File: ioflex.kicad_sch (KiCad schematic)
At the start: 2 parts, among them CN10 DF40C-40DP-0.4V, CN11 DF40C-40DP-0.4V

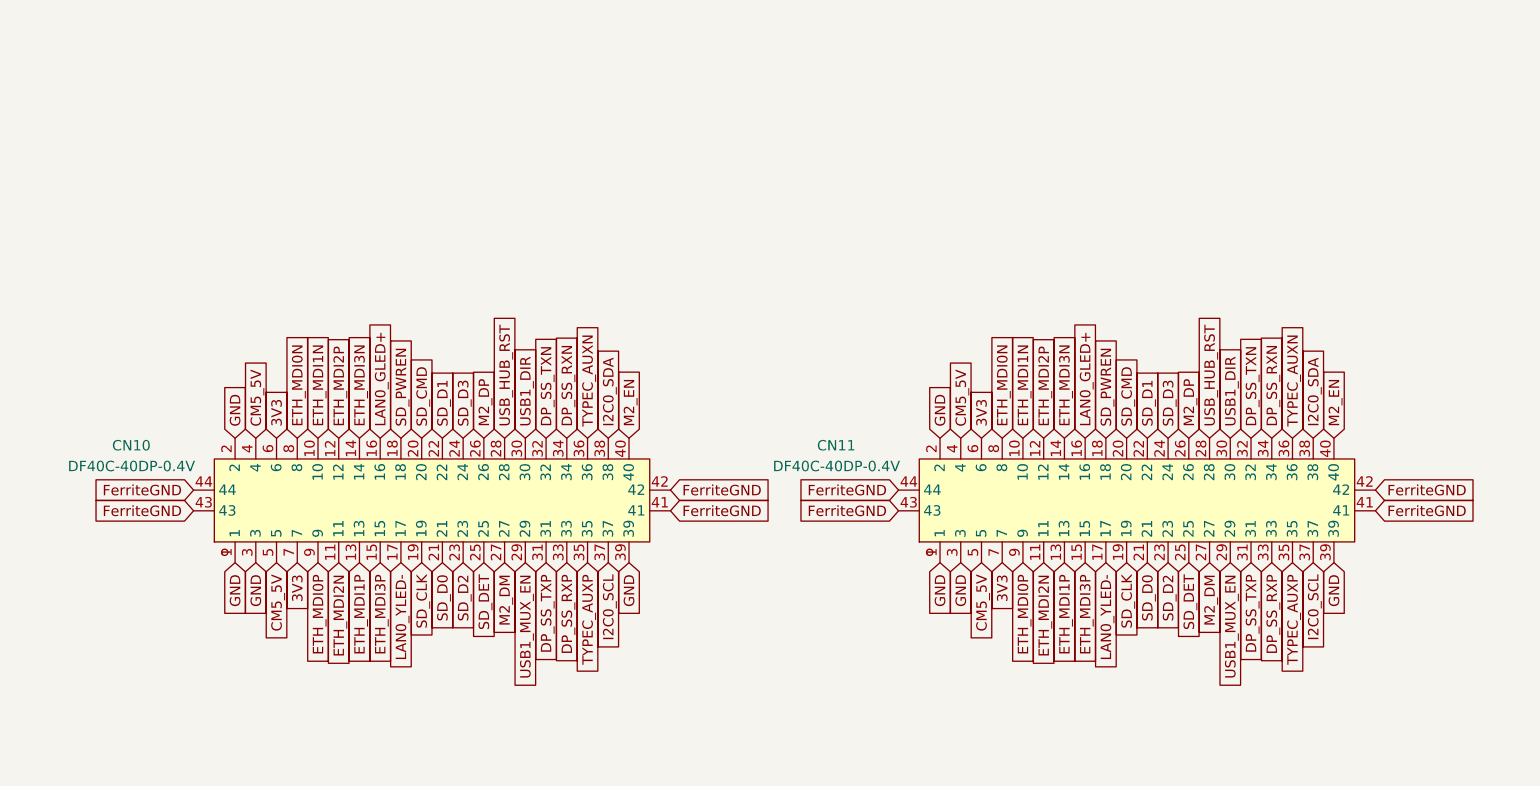
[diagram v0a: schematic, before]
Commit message: finish wiring up usb hub + fix stale nets + address DRC errors
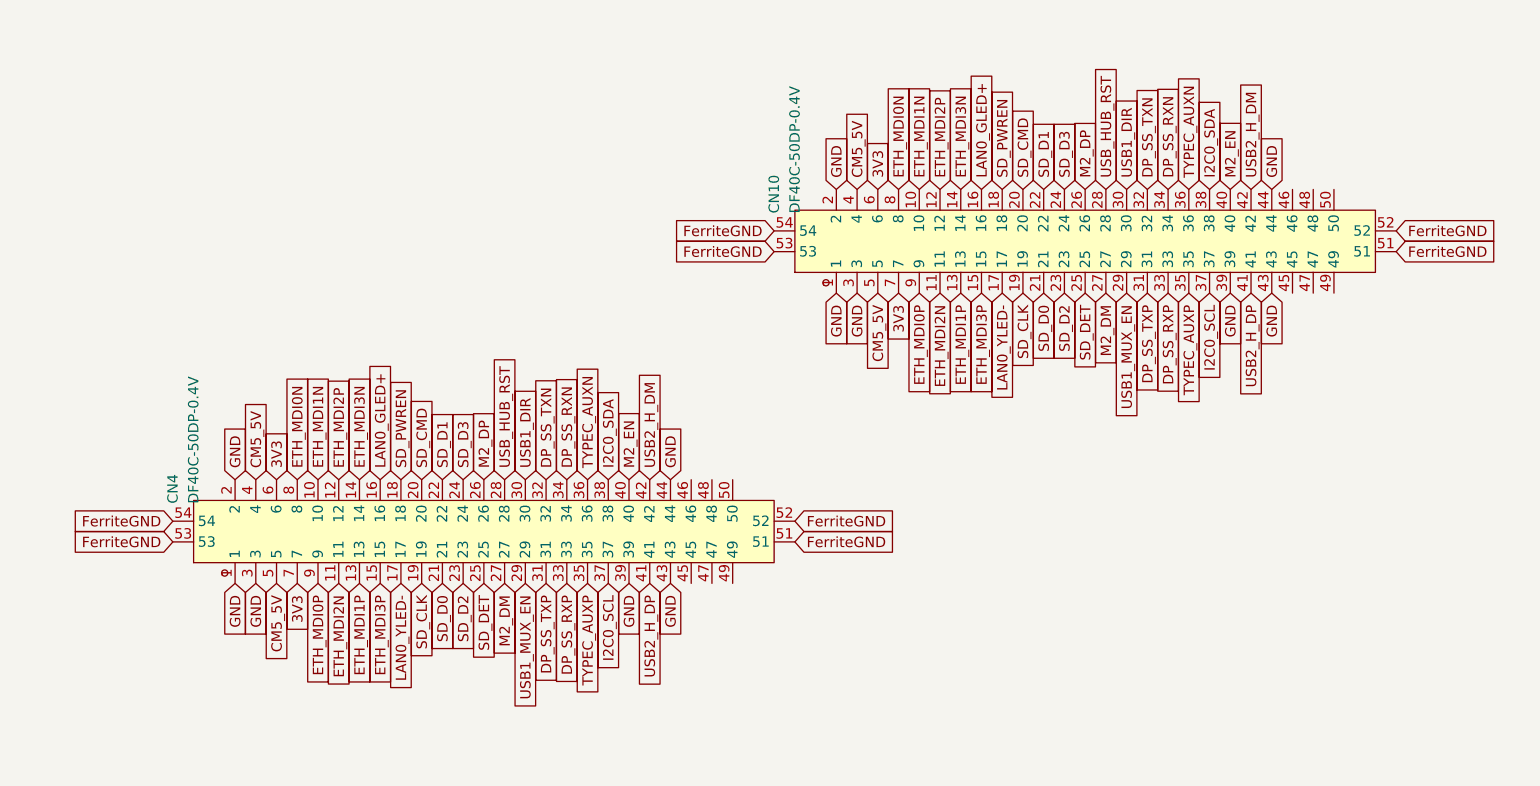
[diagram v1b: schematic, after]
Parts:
- removed CN10, CN11: DF40C-40DP-0.4V, slate113:CONN-SMD_DF40C-40DP-0.4V, symbol slate113:DF40C-40DP-0.4V
- added CN10, CN4: DF40C-50DP-0.4V, slate113:CONN-SMD_DF40C-50DP-0.4V, symbol slate113:DF40C-50DP-0.4V
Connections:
- net 3V3: now also CN10.6, CN10.7, CN4.6, CN4.7
- net CM5_5V: now also CN10.4, CN10.5, CN4.4, CN4.5
- net DP_SS_RXN: now also CN10.34, CN4.34
- net DP_SS_RXP: now also CN10.33, CN4.33
- net DP_SS_TXN: now also CN10.32, CN4.32
- net DP_SS_TXP: now also CN10.31, CN4.31
- net ETH_MDI0N: now also CN10.8, CN4.8
- net ETH_MDI0P: now also CN10.9, CN4.9
- net ETH_MDI1N: now also CN10.10, CN4.10
- net ETH_MDI1P: now also CN10.13, CN4.13
- net ETH_MDI2N: now also CN10.11, CN4.11
- net ETH_MDI2P: now also CN10.12, CN4.12
- net ETH_MDI3N: now also CN10.14, CN4.14
- net ETH_MDI3P: now also CN10.15, CN4.15
- net FerriteGND: now also CN10.51, CN10.52, CN10.53, CN10.54, CN4.51, CN4.52, CN4.53, CN4.54
- net GND: now also CN10.1, CN10.2, CN10.3, CN10.39, CN10.43, CN10.44, CN4.1, CN4.2, CN4.3, CN4.39, CN4.43, CN4.44
- net I2C0_SCL: now also CN10.37, CN4.37
- net I2C0_SDA: now also CN10.38, CN4.38
- net LAN0_GLED+: now also CN10.16, CN4.16
- net LAN0_YLED-: now also CN10.17, CN4.17
- net M2_DM: now also CN10.27, CN4.27
- net M2_DP: now also CN10.26, CN4.26
- net M2_EN: now also CN10.40, CN4.40
- net SD_CLK: now also CN10.19, CN4.19
- net SD_CMD: now also CN10.20, CN4.20
- net SD_D0: now also CN10.21, CN4.21
- net SD_D1: now also CN10.22, CN4.22
- net SD_D2: now also CN10.23, CN4.23
- net SD_D3: now also CN10.24, CN4.24
- net SD_DET: now also CN10.25, CN4.25
- net SD_PWREN: now also CN10.18, CN4.18
- net TYPEC_AUXN: now also CN10.36, CN4.36
- net TYPEC_AUXP: now also CN10.35, CN4.35
- net USB1_DIR: now also CN10.30, CN4.30
- net USB1_MUX_EN: now also CN10.29, CN4.29
- net USB_HUB_RST: now also CN10.28, CN4.28
- new net USB2_H_DM: CN10.42, CN4.42
- new net USB2_H_DP: CN10.41, CN4.41

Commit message: forgot to save
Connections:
- no-connect marks 0 -> 12
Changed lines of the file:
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@@
 	(generator_version "10.0")
 	(paper "A5")
+	(no_connect
+		(at 172.72 45.72)
+	)
+	(no_connect
+		(at 170.18 45.72)
+	)
+	(no_connect
+		(at 93.98 68.58)
+	)
+	(no_connect
+		(at 96.52 68.58)
+	)
+	(no_connect
+		(at 170.18 33.02)
+	)
+	(no_connect
+		(at 172.72 33.02)
+	)
+	(no_connect
+		(at 99.06 81.28)
+	)
+	(no_connect
+		(at 99.06 68.58)
+	)
+	(no_connect
+		(at 167.64 45.72)
+	)
+	(no_connect
+		(at 96.52 81.28)
+	)
+	(no_connect
+		(at 167.64 33.02)
+	)
+	(no_connect
+		(at 93.98 81.28)
+	)
 	(global_label "SD_CLK"
 		(shape input)

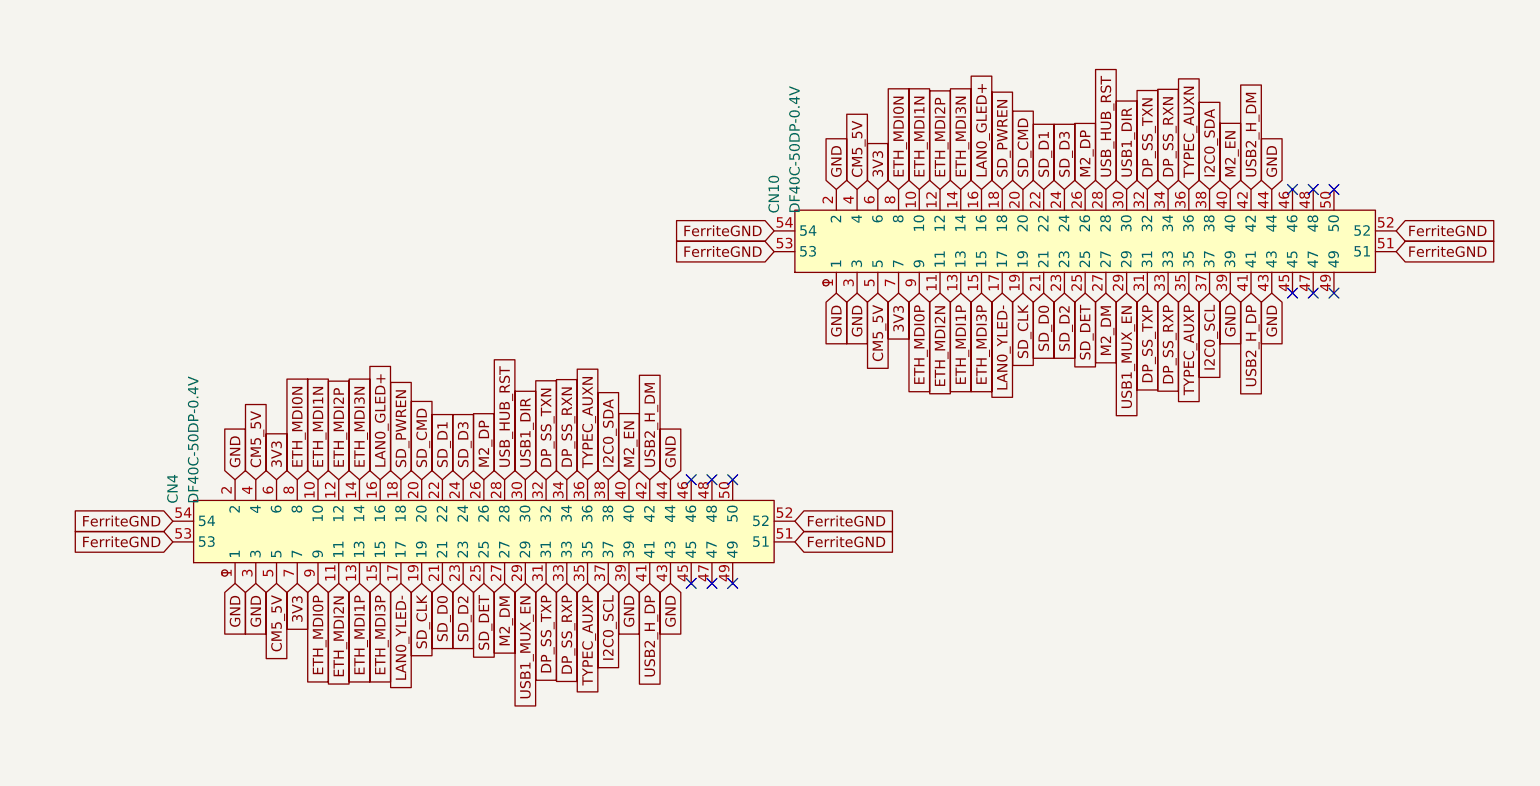
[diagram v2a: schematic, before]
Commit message: finished radio board with load switches and flash, fixed b2b connector, started antenna module and rf sense switching circuit
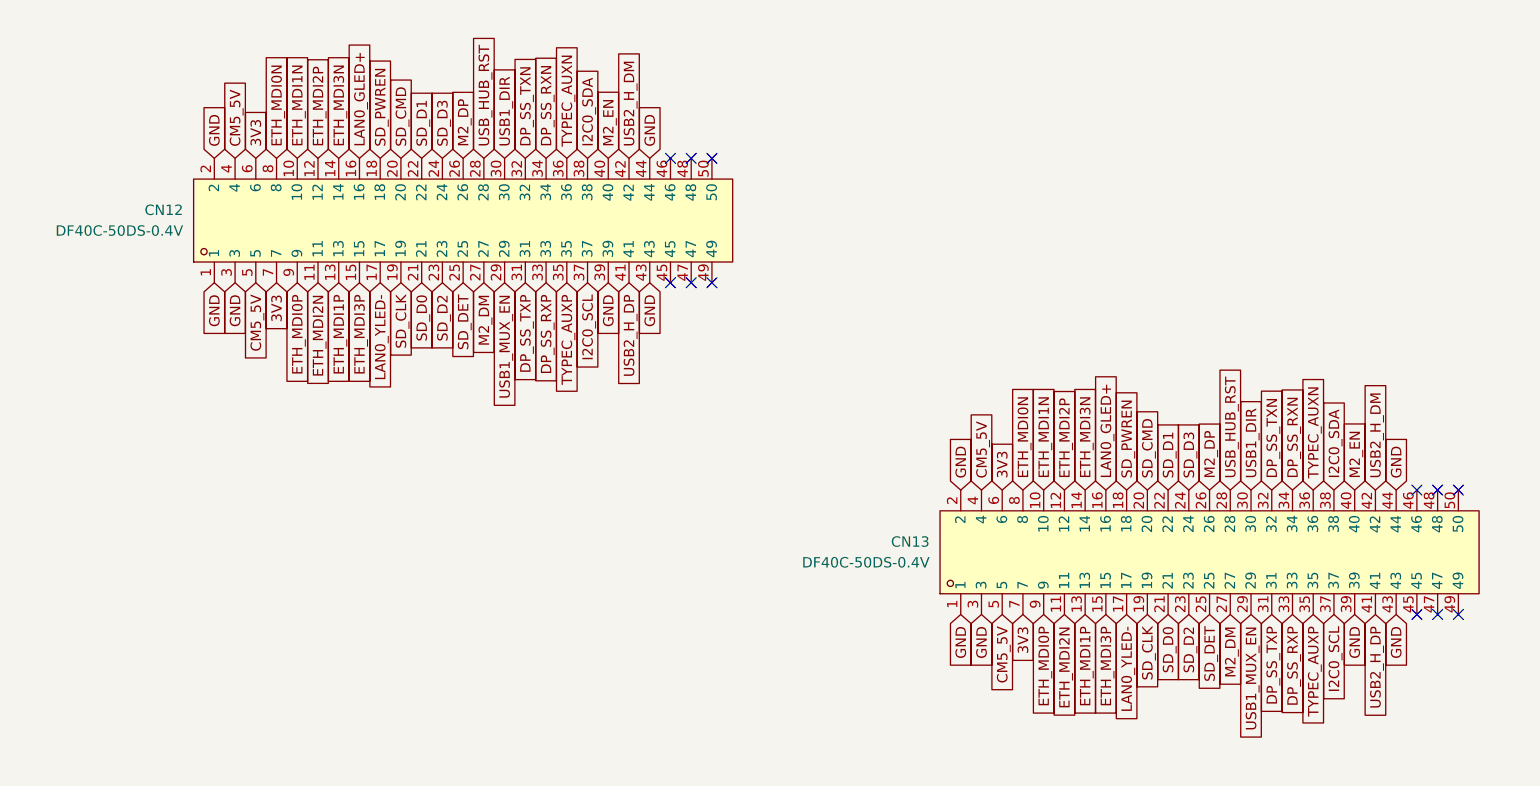
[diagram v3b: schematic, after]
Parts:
- removed CN10, CN4: DF40C-50DP-0.4V, slate113:CONN-SMD_DF40C-50DP-0.4V, symbol slate113:DF40C-50DP-0.4V
- added CN12, CN13: DF40C-50DS-0.4V, slate113:CONN-SMD_DF40C-50DS-0.4V51, symbol slate113:DF40C-50DS-0.4V
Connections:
- net 3V3: now also CN12.6, CN12.7, CN13.6, CN13.7
- net CM5_5V: now also CN12.4, CN12.5, CN13.4, CN13.5
- net DP_SS_RXN: now also CN12.34, CN13.34
- net DP_SS_RXP: now also CN12.33, CN13.33
- net DP_SS_TXN: now also CN12.32, CN13.32
- net DP_SS_TXP: now also CN12.31, CN13.31
- net ETH_MDI0N: now also CN12.8, CN13.8
- net ETH_MDI0P: now also CN12.9, CN13.9
- net ETH_MDI1N: now also CN12.10, CN13.10
- net ETH_MDI1P: now also CN12.13, CN13.13
- net ETH_MDI2N: now also CN12.11, CN13.11
- net ETH_MDI2P: now also CN12.12, CN13.12
- net ETH_MDI3N: now also CN12.14, CN13.14
- net ETH_MDI3P: now also CN12.15, CN13.15
- net GND: now also CN12.1, CN12.2, CN12.3, CN12.39, CN12.43, CN12.44, CN13.1, CN13.2, CN13.3, CN13.39, CN13.43, CN13.44
- net I2C0_SCL: now also CN12.37, CN13.37
- net I2C0_SDA: now also CN12.38, CN13.38
- net LAN0_GLED+: now also CN12.16, CN13.16
- net LAN0_YLED-: now also CN12.17, CN13.17
- net M2_DM: now also CN12.27, CN13.27
- net M2_DP: now also CN12.26, CN13.26
- net M2_EN: now also CN12.40, CN13.40
- net SD_CLK: now also CN12.19, CN13.19
- net SD_CMD: now also CN12.20, CN13.20
- net SD_D0: now also CN12.21, CN13.21
- net SD_D1: now also CN12.22, CN13.22
- net SD_D2: now also CN12.23, CN13.23
- net SD_D3: now also CN12.24, CN13.24
- net SD_DET: now also CN12.25, CN13.25
- net SD_PWREN: now also CN12.18, CN13.18
- net TYPEC_AUXN: now also CN12.36, CN13.36
- net TYPEC_AUXP: now also CN12.35, CN13.35
- net USB1_DIR: now also CN12.30, CN13.30
- net USB1_MUX_EN: now also CN12.29, CN13.29
- net USB2_H_DM: now also CN12.42, CN13.42
- net USB2_H_DP: now also CN12.41, CN13.41
- net USB_HUB_RST: now also CN12.28, CN13.28

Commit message: finished rf sense and io board closure, added audio system with pcm and three spdt switches, made changes tp lte module, added ldo and sd/sim slot, updated m.2/audio schematics, added new mic msop qfn sot footprints, and added a protection system for non EM06-A Cards
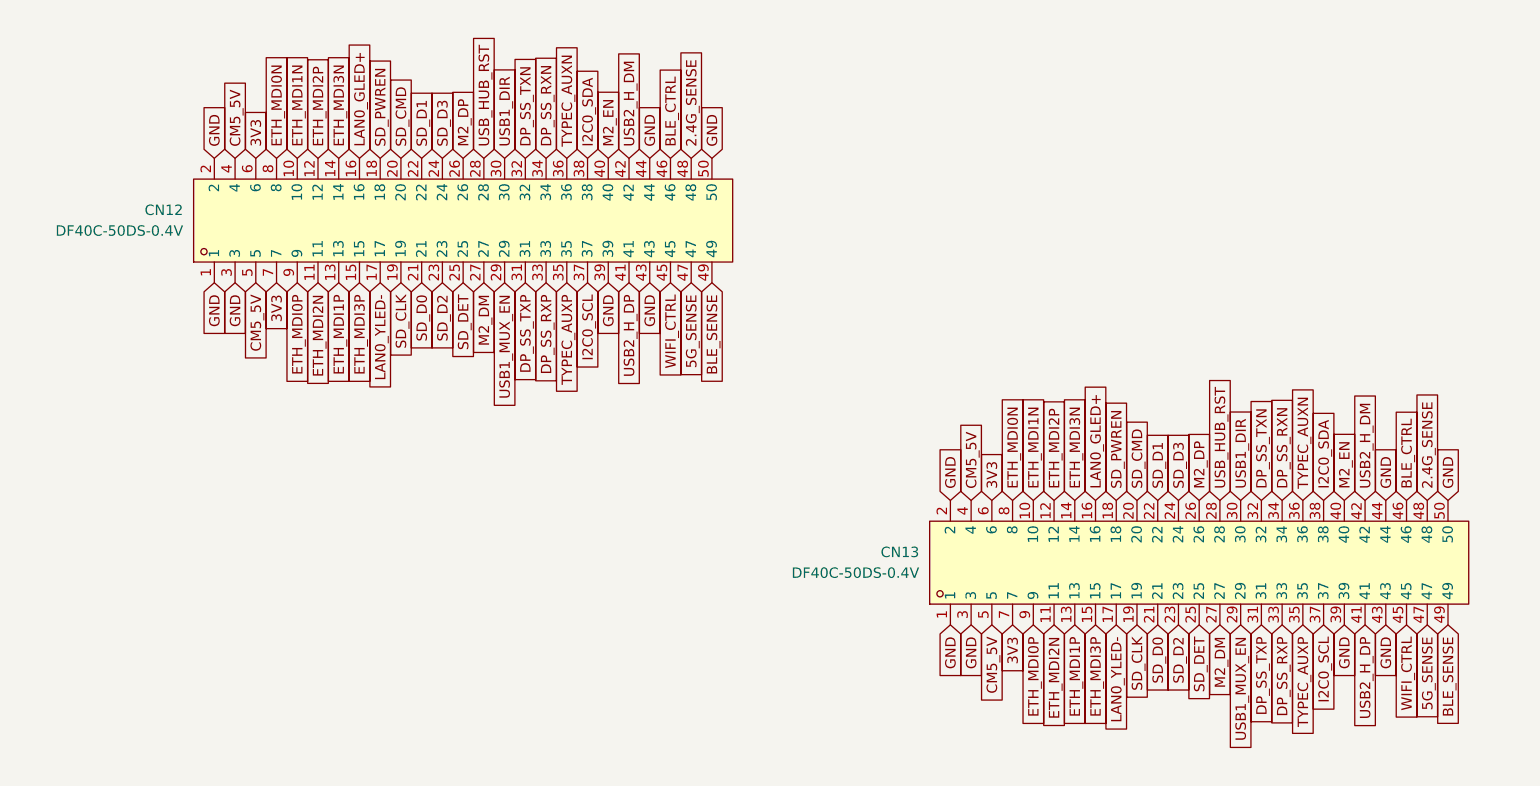
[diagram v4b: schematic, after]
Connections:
- net GND: now also CN12.50, CN13.50
- net WIFI_CTRL: now reaches CN13.45
- net WIFI_CTRL: now also CN12.45
- net BLE_CTRL: now reaches CN13.46
- net BLE_CTRL: now also CN12.46
- net 5G_SENSE: now reaches CN13.47
- net 5G_SENSE: now also CN12.47
- net 2.4G_SENSE: now reaches CN13.48
- net 2.4G_SENSE: now also CN12.48
- net BLE_SENSE: now reaches CN13.49
- net BLE_SENSE: now also CN12.49
- no-connect marks 12 -> 0

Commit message: finished slateconnect i2c gpio expander, completed led status bar schematic, fixed all drc errors, started assigning footprints and started bom
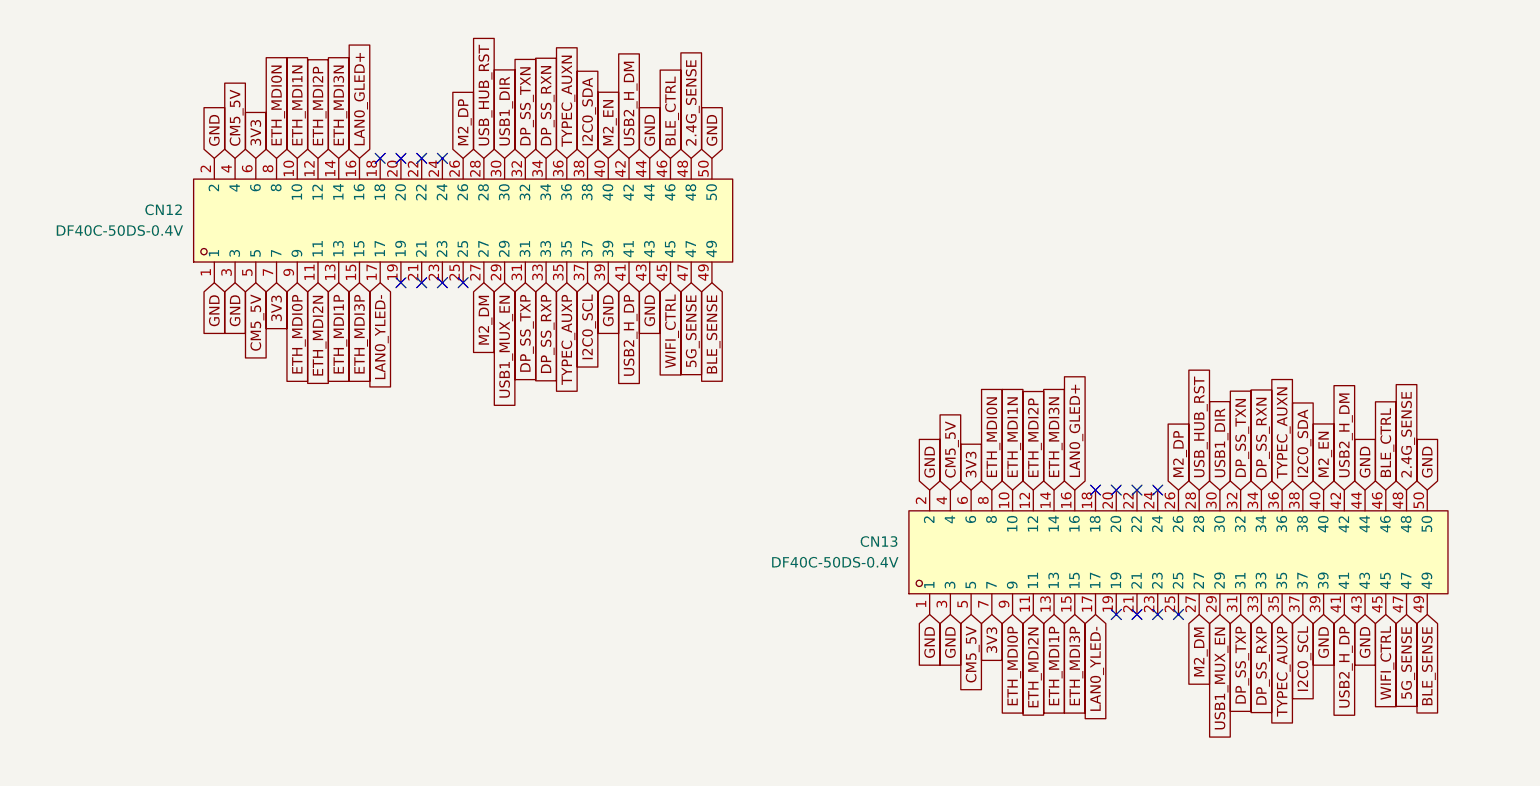
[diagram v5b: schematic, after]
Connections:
- net SD_CLK: no longer names the net of CN13.19
- net SD_CLK: no longer CN12.19
- net SD_CMD: no longer names the net of CN13.20
- net SD_CMD: no longer CN12.20
- net SD_D0: no longer names the net of CN13.21
- net SD_D0: no longer CN12.21
- net SD_D1: no longer names the net of CN13.22
- net SD_D1: no longer CN12.22
- net SD_D2: no longer names the net of CN13.23
- net SD_D2: no longer CN12.23
- net SD_D3: no longer names the net of CN13.24
- net SD_D3: no longer CN12.24
- net SD_DET: no longer names the net of CN13.25
- net SD_DET: no longer CN12.25
- net SD_PWREN: no longer names the net of CN13.18
- net SD_PWREN: no longer CN12.18
- no-connect marks 0 -> 16
